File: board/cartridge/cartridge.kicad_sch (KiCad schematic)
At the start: 34 parts, among them J1 TF-115-BCP9, J2 HC-TYPE-C-16P-01B, Q1 DMG2301L, SW1 K3-1410S, SW2 K3-1410S, U1 AMS1117-3.3, U10 TPS2041B, U11 LM66100DCK, U12 LM66100DCK, U2 ESP32-S3-WROOM-1U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

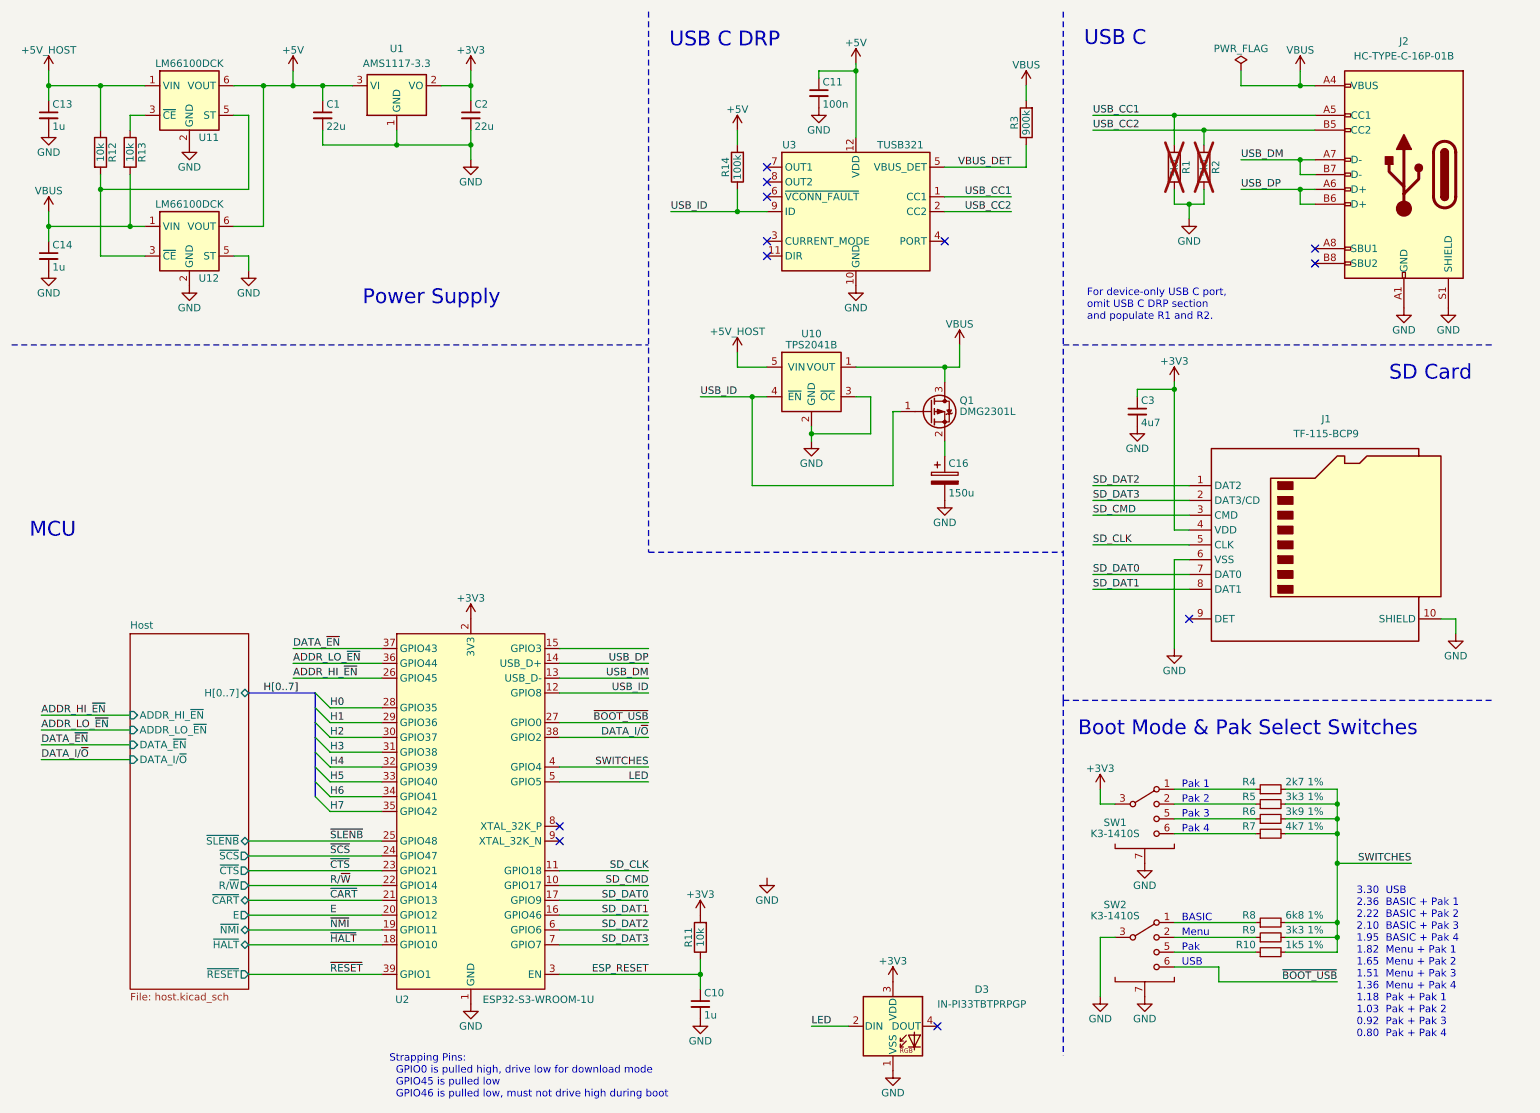
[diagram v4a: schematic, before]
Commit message: Finish adding solder links for configuration.
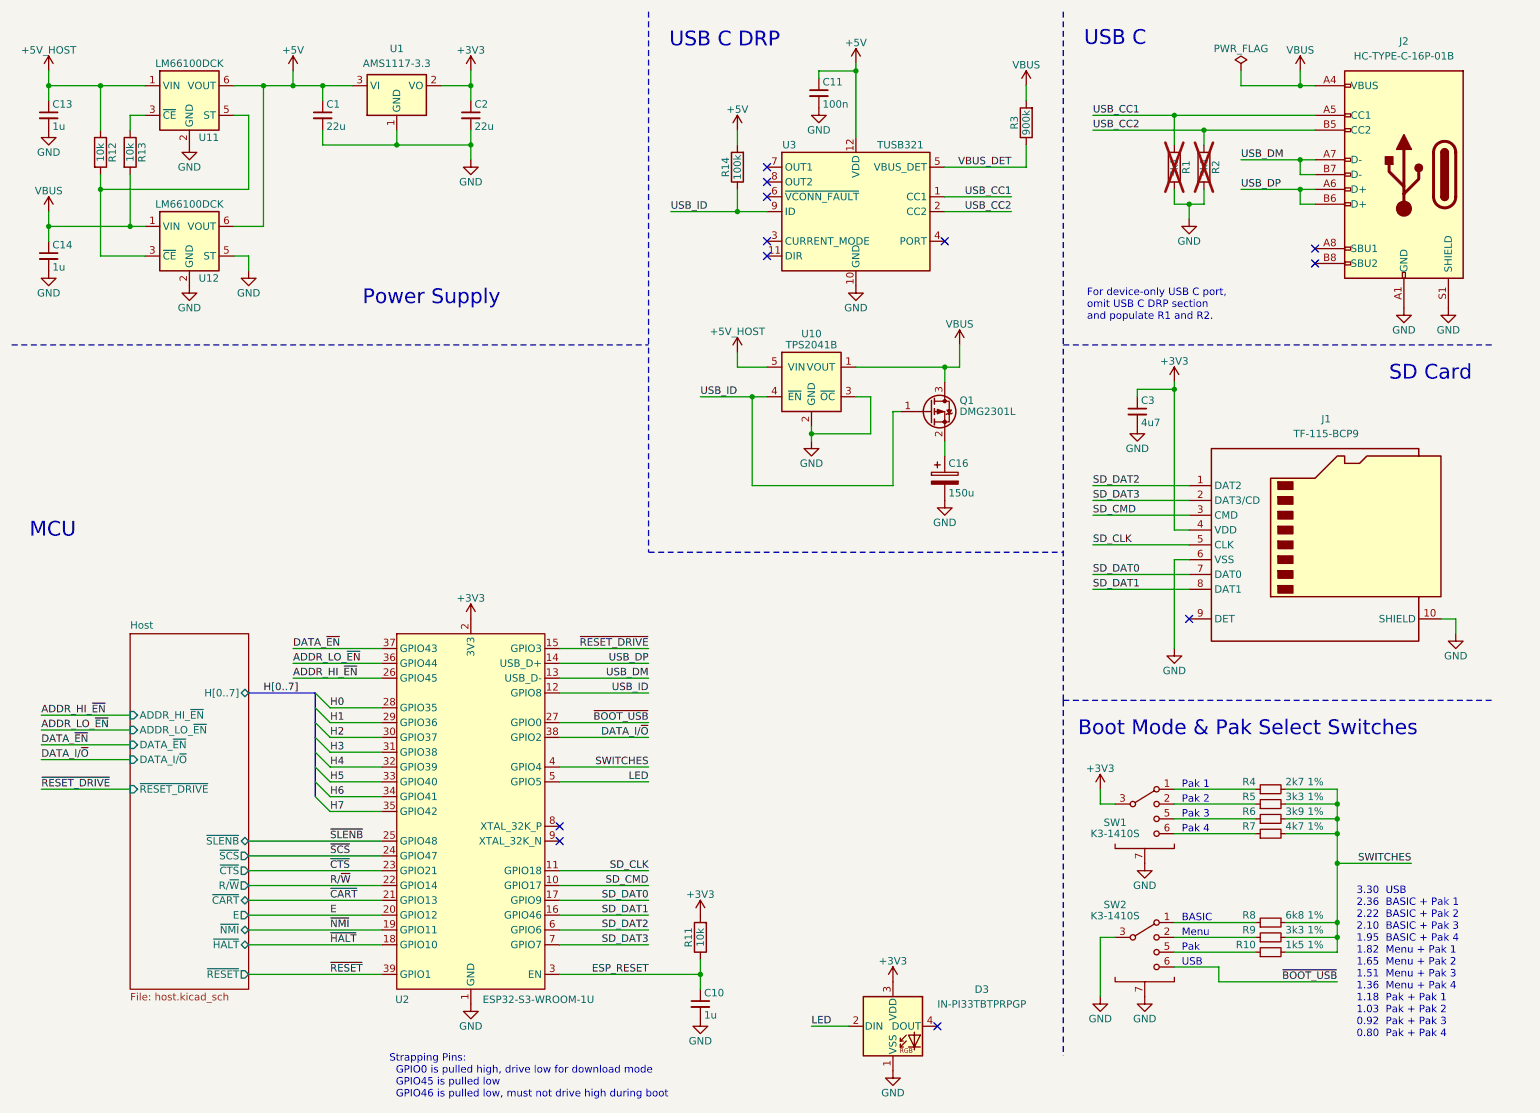
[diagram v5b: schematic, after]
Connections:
- net ~{RESET_DRIVE}: now reaches U2.15 (GPIO3)
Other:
- sheet Host ports: added ~{RESET_DRIVE}; removed none
- company: © 2023 Sam Hanes, licensed CERN-OHL-W v2 -> © 2023-2025 Sam Hanes, licensed CERN-OHL-W v2

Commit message: Ensure all parts are available from DigiKey and JLCPCB.
This switches the symbols and footprints to the more widely available
parts sourced from DigiKey. Parts also have an LCSC catalog number,
which may be the same part or a cheaper compatible clone.
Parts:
- D3: DigiKey (none) -> 1830-1208-1-ND; LCSC (none) -> C5259062
- J1: value TF-115-BCP9 -> Attend 112J; footprint 0Project:XUNPU_TF-115-BCP9 -> 0Project:Attend_112J; DigiKey (none) -> 4827-112J-TDAR-R01CT-ND; LCSC C720505 -> C393941
- J2: value HC-TYPE-C-16P-01B -> GCT USB4105; footprint 0Project:HC-TYPE-C-16P-01B -> 0Project:GCT_USB4105; DigiKey (none) -> 2073-USB4105-GF-ACT-ND
- SW1, SW2: value K3-1410S -> CUS-14TB; footprint 0Project:K3-1410S -> 0Project:Nidec_CUS-14TB; symbol 0Project:K3-1410S -> 0Project:Nidec_CUS-14TB; DigiKey (none) -> 563-1104-1-ND
- U1: DigiKey (none) -> 5399-AMS1117-3.3SOT-223CT-ND
- U10: DigiKey (none) -> 296-21263-1-ND; LCSC (none) -> C51386
- U11, U12: DigiKey (none) -> 296-53541-1-ND; LCSC (none) -> C2869734
- U2: DigiKey (none) -> 1965-ESP32-S3-WROOM-1U-N16R2CT-ND; LCSC (none) -> C3013945
- U3: DigiKey (none) -> 296-42400-1-ND; LCSC (none) -> C139392
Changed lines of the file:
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@@
 			)
 		)
+		(property "DigiKey" "5399-AMS1117-3.3SOT-223CT-ND"
+			(at 78.74 25.4 0)
+			(effects
+				(font
+					(size 1.27 1.27)
+				)
+				(hide yes)
+			)
+		)
 		(pin "3"
 		)
@@
 			)
 		)
+		(property "LCSC" "C2869734"
+			(at 43.18 27.94 0)
+			(effects
+				(font
+					(size 1.27 1.27)
+				)
+				(hide yes)
+			)
+		)
+		(property "DigiKey" "296-53541-1-ND"
+			(at 43.18 27.94 0)
+			(effects
+				(font
+					(size 1.27 1.27)
+				)
+				(hide yes)
+			)
+		)
 		(pin "6"
 		)
@@
 	)
 	(symbol
-		(lib_id "0Project:K3-1410S")
+		(lib_id "0Project:Nidec_CUS-14TB")
 		(at 207.01 148.59 0)
 		(unit 1)
@@
 			)
 		)
-		(property "Value" "K3-1410S"
+		(property "Value" "CUS-14TB"
 			(at 201.93 153.67 0)
 			(effects
@@
 			)
 		)
-		(property "Footprint" "0Project:K3-1410S"
+		(property "Footprint" "0Project:Nidec_CUS-14TB"
 			(at 207.01 137.795 0)
 			(effects
@@
 			)
 		)
-		(property "Datasheet" "https://datasheet.lcsc.com/lcsc/2108131730_Korean-Hroparts-Elec-K3-1410S_C145846.pdf"
+		(property "Datasheet" "https://www.nidec-components.com/e/catalog/switch/cus.pdf"
 			(at 207.01 139.7 0)
 			(effects
@@
 			)
 		)
-		(property "Description" ""
+		(property "Description" "Switch, four position, single pole quad throw, 4 position switch, SP4T"
 			(at 207.01 148.59 0)
 			(effects
@@
 			)
 		)
+		(property "DigiKey" "563-1104-1-ND"
+			(at 207.01 148.59 0)
+			(effects
+				(font
+					(size 1.27 1.27)
+				)
+				(hide yes)
+			)
+		)
 		(pin "3"
 		)
@@
 	)
 	(symbol
-		(lib_id "0Project:K3-1410S")
+		(lib_id "0Project:Nidec_CUS-14TB")
 		(at 207.01 171.45 0)
 		(unit 1)
@@
 			)
 		)
-		(property "Value" "K3-1410S"
+		(property "Value" "CUS-14TB"
 			(at 201.93 167.767 0)
 			(effects
@@
 			)
 		)
-		(property "Footprint" "0Project:K3-1410S"
+		(property "Footprint" "0Project:Nidec_CUS-14TB"
 			(at 207.01 160.655 0)
 			(effects
@@
 			)
 		)
-		(property "Datasheet" "https://datasheet.lcsc.com/lcsc/2108131730_Korean-Hroparts-Elec-K3-1410S_C145846.pdf"
+		(property "Datasheet" "https://www.nidec-components.com/e/catalog/switch/cus.pdf"
 			(at 207.01 162.56 0)
 			(effects
@@
 			)
 		)
-		(property "Description" ""
+		(property "Description" "Switch, four position, single pole quad throw, 4 position switch, SP4T"
 			(at 207.01 171.45 0)
 			(effects
@@
 			)
 		)
+		(property "DigiKey" "563-1104-1-ND"
+			(at 207.01 171.45 0)
+			(effects
+				(font
+					(size 1.27 1.27)
+				)
+				(hide yes)
+			)
+		)
 		(pin "3"
 		)
@@
 			)
 		)
+		(property "LCSC" "C2869734"
+			(at 43.18 52.07 0)
+			(effects
+				(font
+					(size 1.27 1.27)
+				)
+				(hide yes)
+			)
+		)
+		(property "DigiKey" "296-53541-1-ND"
+			(at 43.18 52.07 0)
+			(effects
+				(font
+					(size 1.27 1.27)
+				)
+				(hide yes)
+			)
+		)
 		(pin "6"
 		)
@@
 			)
 		)
-		(property "Value" "TF-115-BCP9"
+		(property "Value" "Attend 112J"
 			(at 238.125 85.09 0)
 			(effects
@@
 			)
 		)
-		(property "Footprint" "0Project:XUNPU_TF-115-BCP9"
+		(property "Footprint" "0Project:Attend_112J"
 			(at 289.56 86.36 0)
 			(effects
@@
 			)
 		)
-		(property "Datasheet" "https://datasheet.lcsc.com/lcsc/2109061830_XUNPU-TF-115-BCP9_C720505.pdf"
+		(property "Datasheet" "https://www.attend.com.tw/data/download/file/112J-TDAR-R01_B_3.pdf"
 			(at 237.49 101.6 0)
 			(effects
@@
 			)
 		)
-		(property "LCSC" "C720505"
+		(property "LCSC" "C393941"
+			(at 237.49 104.14 0)
+			(effects
+				(font
+					(size 1.27 1.27)
+				)
+				(hide yes)
+			)
+		)
+		(property "DigiKey" "4827-112J-TDAR-R01CT-ND"
 			(at 237.49 104.14 0)
 			(effects
@@
 			)
 		)
+		(property "LCSC" "C3013945"
+			(at 91.44 149.86 0)
+			(effects
+				(font
+					(size 1.27 1.27)
+				)
+				(hide yes)
+			)
+		)
+		(property "DigiKey" "1965-ESP32-S3-WROOM-1U-N16R2CT-ND"
+			(at 91.44 149.86 0)
+			(effects
+				(font
+					(size 1.27 1.27)
+				)
+				(hide yes)
+			)
+		)
 		(pin "33"
 		)
@@
 			)
 		)
+		(property "LCSC" "C139392"
+			(at 157.48 46.99 0)
+			(effects
+				(font
+					(size 1.27 1.27)
+				)
+				(hide yes)
+			)
+		)
+		(property "DigiKey" "296-42400-1-ND"
+			(at 157.48 46.99 0)
+			(effects
+				(font
+					(size 1.27 1.27)
+				)
+				(hide yes)
+			)
+		)
 		(pin "5"
 		)
@@
 			)
 		)
-		(property "Datasheet" ""
+		(property "Datasheet" "https://www.inolux-corp.com/datasheet/SMDLED/Addressable%20LED/IN-PI33TBTPRPGPB_v1.2.pdf"
 			(at 166.37 196.215 0)
 			(effects
@@
 			)
 		)
+		(property "LCSC" "C5259062"
+			(at 163.83 186.69 0)
+			(effects
+				(font
+					(size 1.27 1.27)
+				)
+				(hide yes)
+			)
+		)
+		(property "DigiKey" "1830-1208-1-ND"
+			(at 163.83 186.69 0)
+			(effects
+				(font
+					(size 1.27 1.27)
+				)
+				(hide yes)
+			)
+		)
 		(pin "1"
 		)
@@
 			)
 		)
+		(property "LCSC" "C51386"
+			(at 149.86 73.66 0)
+			(effects
+				(font
+					(size 1.27 1.27)
+				)
+				(hide yes)
+			)
+		)
+		(property "DigiKey" "296-21263-1-ND"
+			(at 149.86 73.66 0)
+			(effects
+				(font
+					(size 1.27 1.27)
+				)
+				(hide yes)
+			)
+		)
 		(pin "2"
 		)
@@
 			)
 		)
-		(property "Value" "HC-TYPE-C-16P-01B"
+		(property "Value" "GCT USB4105"
 			(at 251.46 20.32 0)
 			(effects
@@
 			)
 		)
-		(property "Footprint" "0Project:HC-TYPE-C-16P-01B"
+		(property "Footprint" "0Project:GCT_USB4105"
 			(at 247.65 40.64 0)
 			(effects
@@
 			)
 		)
-		(property "Datasheet" "https://datasheet.lcsc.com/lcsc/2211161000_HCTL-HC-TYPE-C-16P-01B_C2894898.pdf"
+		(property "Datasheet" "https://gct.co/files/drawings/usb4105.pdf"
 			(at 247.65 40.64 0)
 			(effects
@@
 			(at 251.46 40.64 0)
 			(effects
+				(font
+					(size 1.27 1.27)
+				)
+				(hide yes)
+			)
+		)
+		(property "DigiKey" "2073-USB4105-GF-ACT-ND"
+			(at 251.46 40.64 0)
+			(effects

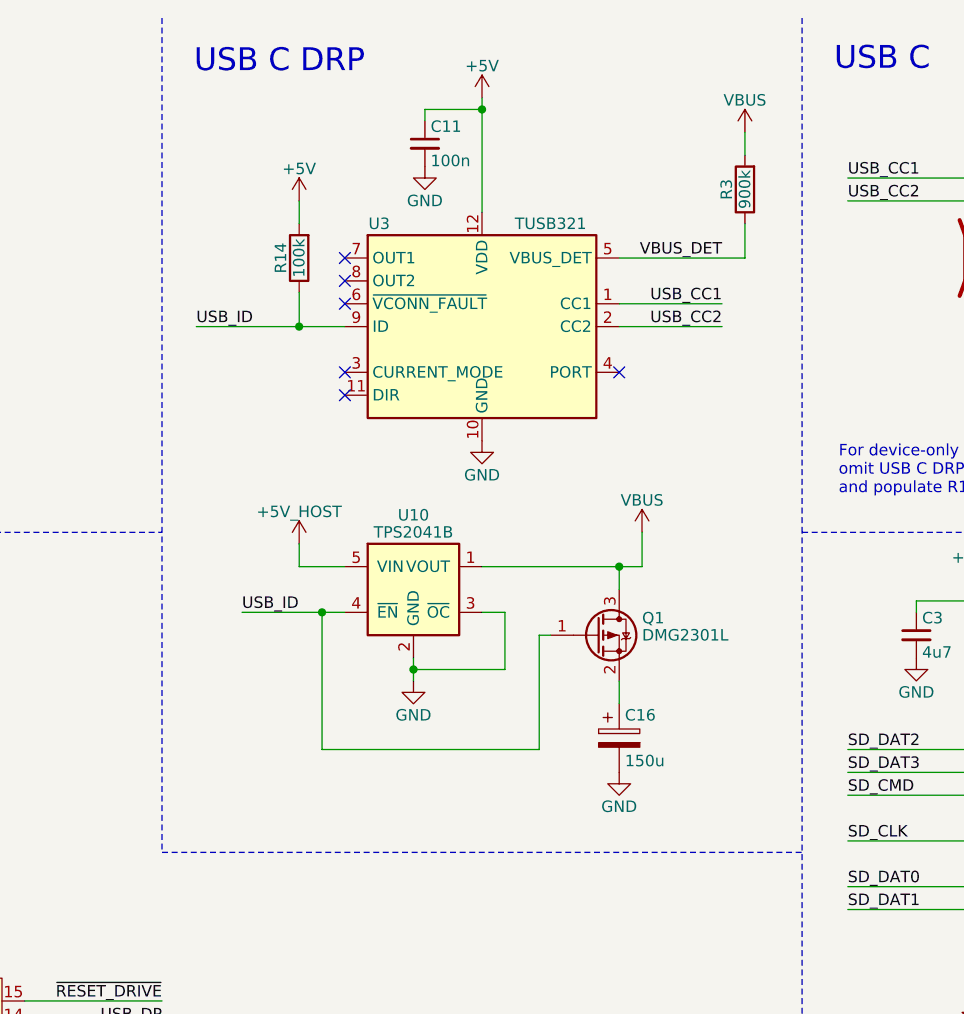
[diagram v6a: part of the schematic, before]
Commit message: Remove USB host bulk capacitor.
I'm reasonably certain the bulk capacitor referred to by the USB 2.0
spec is only actually required for multi-port hubs.
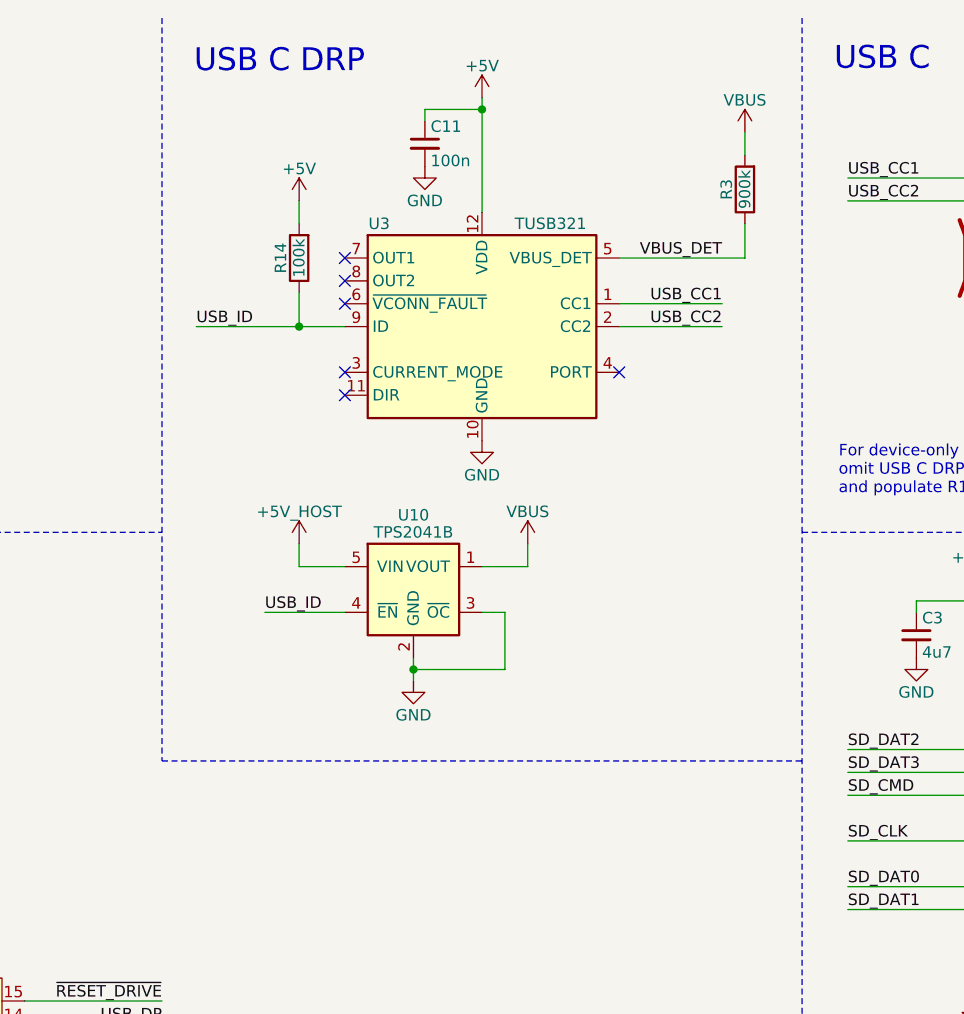
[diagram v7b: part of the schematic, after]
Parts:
- removed C16: 150u, Capacitor_Tantalum_SMD:CP_EIA-3528-21_Kemet-B, symbol Device:C_Polarized
- removed Q1: DMG2301L, 0Project:SOT-23, symbol Transistor_FET:DMG2301L

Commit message: Fix issues with ESP32-S3-WROOM-1U library footprint.
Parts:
- U2: footprint RF_Module:ESP32-S3-WROOM-1U -> 0Project:ESP32-S3-WROOM-1U
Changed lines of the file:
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@@
 			)
 		)
-		(property "Footprint" "RF_Module:ESP32-S3-WROOM-1U"
+		(property "Footprint" "0Project:ESP32-S3-WROOM-1U"
 			(at 91.44 198.12 0)
 			(effects
